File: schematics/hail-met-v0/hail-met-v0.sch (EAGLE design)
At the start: 110 parts, among them IC1 MCP73871, J1 AVR_SPI_PRG_6PTH, U1 ATMEGA328P, Y1 16MHZ

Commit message: ordered pcb
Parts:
- renumbered LED0-IR to LED4-IR
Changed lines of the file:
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@@
 <?xml version="1.0" encoding="utf-8"?>
 <!DOCTYPE eagle SYSTEM "eagle.dtd">
-<eagle version="7.1.0">
+<eagle version="6.5.0">
 <drawing>
 <settings>
@@
 <part name="LED7-CS" library="SparkFun-Connectors" deviceset="M02" device="PTH"/>
 <part name="LED0-IL" library="SparkFun-Connectors" deviceset="M02" device="PTH"/>
-<part name="LED0-IR" library="SparkFun-Connectors" deviceset="M02" device="PTH"/>
+<part name="LED4-IR" library="SparkFun-Connectors" deviceset="M02" device="PTH"/>
 <part name="LED_CREE" library="SparkFun-Connectors" deviceset="M02" device="PTH"/>
 <part name="P+8" library="SparkFun" deviceset="3.3V" device=""/>
@@
 <instance part="LED7-CS" gate="G$1" x="167.64" y="-83.82" rot="R180"/>
 <instance part="LED0-IL" gate="G$1" x="142.24" y="-22.86" rot="R180"/>
-<instance part="LED0-IR" gate="G$1" x="167.64" y="-22.86" rot="R180"/>
+<instance part="LED4-IR" gate="G$1" x="167.64" y="-22.86" rot="R180"/>
 <instance part="LED_CREE" gate="G$1" x="99.06" y="-15.24" rot="R180"/>
 <instance part="P+8" gate="G$1" x="127" y="-38.1"/>
@@
 </segment>
 <segment>
-<pinref part="LED0-IR" gate="G$1" pin="1"/>
+<pinref part="LED4-IR" gate="G$1" pin="1"/>
 <pinref part="P+17" gate="G$1" pin="3.3V"/>
 <wire x1="160.02" y1="-22.86" x2="154.94" y2="-22.86" width="0.1524" layer="91"/>
@@
 <net name="N$66" class="0">
 <segment>
-<pinref part="LED0-IR" gate="G$1" pin="2"/>
+<pinref part="LED4-IR" gate="G$1" pin="2"/>
 <pinref part="R23" gate="G$1" pin="1"/>
 </segment>

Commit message: updated schematics (v0, v1) and datasheets
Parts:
- R11: value 100K -> 8K
- R3: value (none) -> 270K
- R4: value (none) -> 100K
- RT1: value (none) -> 0
- RT2: value (none) -> 80K
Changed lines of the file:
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@@
 <?xml version="1.0" encoding="utf-8"?>
 <!DOCTYPE eagle SYSTEM "eagle.dtd">
-<eagle version="6.5.0">
+<eagle version="7.1.0">
 <drawing>
 <settings>
@@
 <part name="R5" library="SparkFun-Passives" deviceset="RESISTOR" device="0805-RES" value="10K"/>
 <part name="R6" library="SparkFun-Passives" deviceset="RESISTOR" device="0805-RES" value="10K"/>
-<part name="R3" library="SparkFun-Passives" deviceset="RESISTOR" device="0805-RES"/>
-<part name="R4" library="SparkFun-Passives" deviceset="RESISTOR" device="0805-RES"/>
+<part name="R3" library="SparkFun-Passives" deviceset="RESISTOR" device="0805-RES" value="270K"/>
+<part name="R4" library="SparkFun-Passives" deviceset="RESISTOR" device="0805-RES" value="100K"/>
 <part name="R7" library="SparkFun-Passives" deviceset="RESISTOR" device="0805-RES" value="2K"/>
-<part name="R11" library="SparkFun-Passives" deviceset="RESISTOR" device="0805-RES" value="100K"/>
-<part name="RT1" library="SparkFun-Passives" deviceset="RESISTOR" device="0805-RES"/>
-<part name="RT2" library="SparkFun-Passives" deviceset="RESISTOR" device="0805-RES"/>
+<part name="R11" library="SparkFun-Passives" deviceset="RESISTOR" device="0805-RES" value="8K"/>
+<part name="RT1" library="SparkFun-Passives" deviceset="RESISTOR" device="0805-RES" value="0"/>
+<part name="RT2" library="SparkFun-Passives" deviceset="RESISTOR" device="0805-RES" value="80K"/>
 <part name="C7" library="SparkFun-Passives" deviceset="CAP" device="0805" value="10uF"/>
 <part name="C8" library="SparkFun-Passives" deviceset="CAP" device="0805" value="22pF"/>

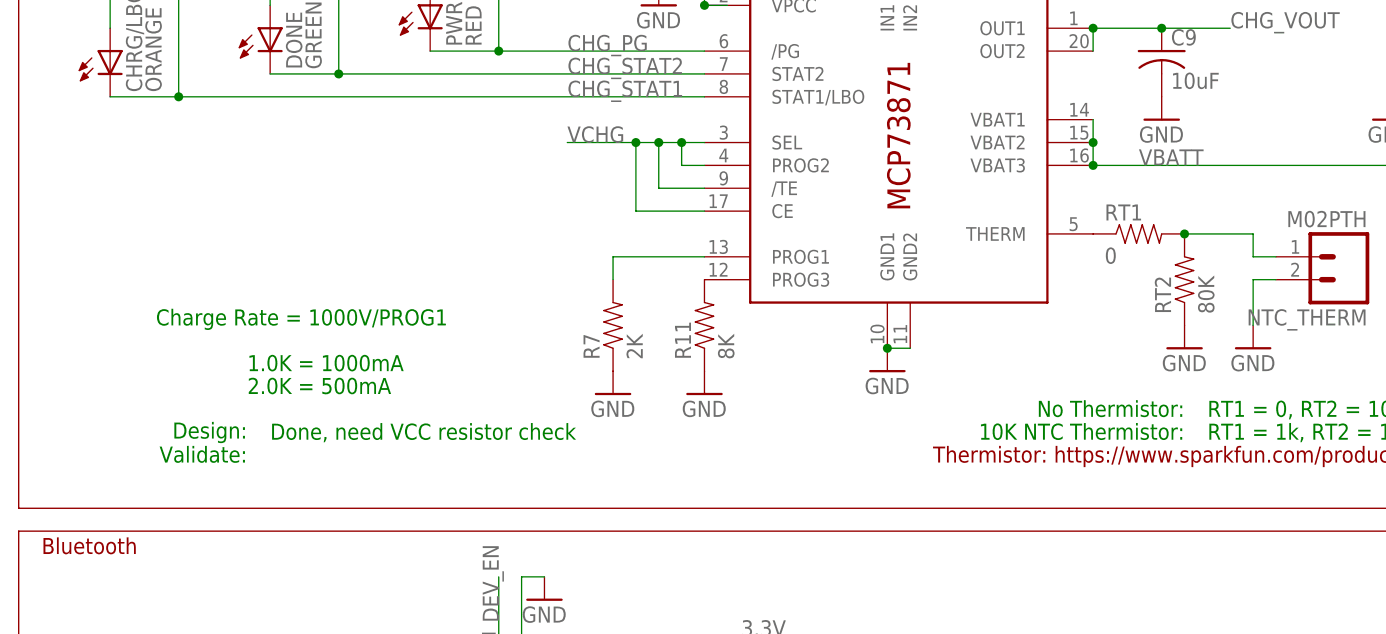
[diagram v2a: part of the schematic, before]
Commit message: updated schematic with charge termination current resistor
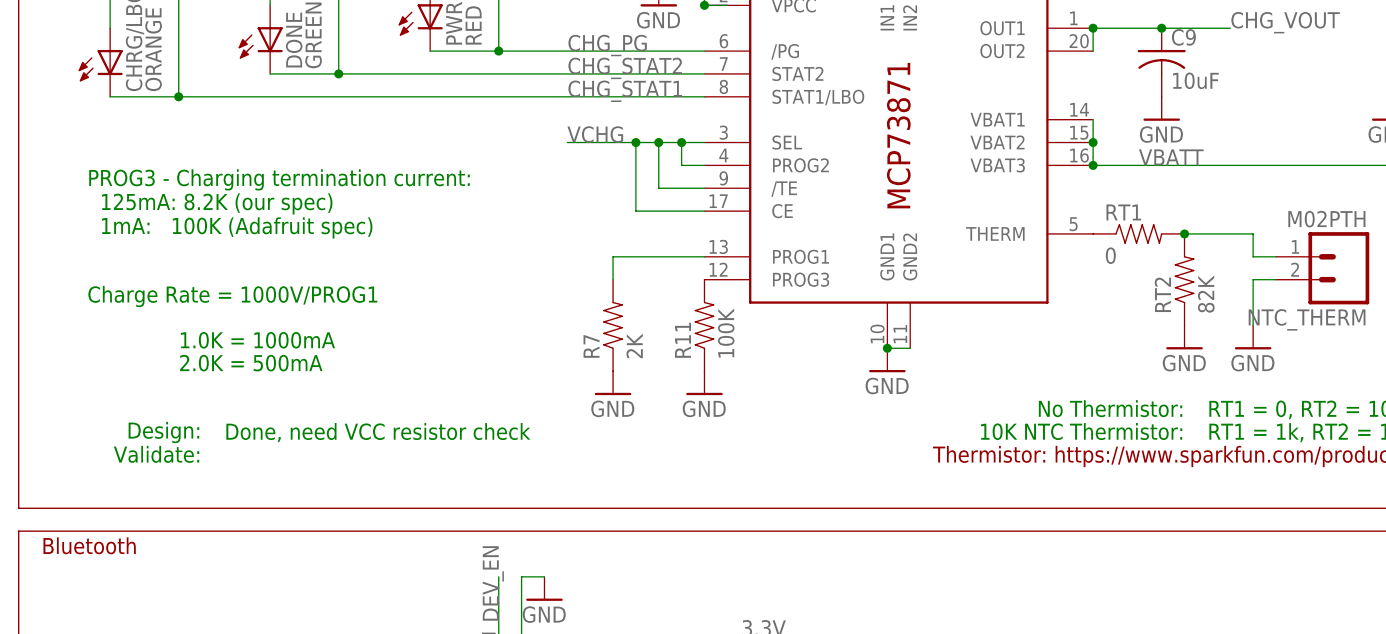
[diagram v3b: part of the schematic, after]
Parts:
- R11: value 8K -> 100K
- RT2: value 80K -> 82K
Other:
- note added: "PROG3 - Charging termination current: 125mA: 8.2K (our spec) 1mA: 100K (Adafruit spec)"
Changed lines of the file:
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@@
 <part name="R4" library="SparkFun-Passives" deviceset="RESISTOR" device="0805-RES" value="100K"/>
 <part name="R7" library="SparkFun-Passives" deviceset="RESISTOR" device="0805-RES" value="2K"/>
-<part name="R11" library="SparkFun-Passives" deviceset="RESISTOR" device="0805-RES" value="8K"/>
+<part name="R11" library="SparkFun-Passives" deviceset="RESISTOR" device="0805-RES" value="100K"/>
 <part name="RT1" library="SparkFun-Passives" deviceset="RESISTOR" device="0805-RES" value="0"/>
-<part name="RT2" library="SparkFun-Passives" deviceset="RESISTOR" device="0805-RES" value="80K"/>
+<part name="RT2" library="SparkFun-Passives" deviceset="RESISTOR" device="0805-RES" value="82K"/>
 <part name="C7" library="SparkFun-Passives" deviceset="CAP" device="0805" value="10uF"/>
 <part name="C8" library="SparkFun-Passives" deviceset="CAP" device="0805" value="22pF"/>
@@
 <text x="-55.88" y="5.08" size="1.778" layer="91" distance="5">RT1 = 0, RT2 = 10K</text>
 <text x="-55.88" y="2.54" size="1.778" layer="91" distance="5">RT1 = 1k, RT2 = 150k</text>
-<text x="-172.72" y="15.24" size="1.778" layer="91" distance="5">Charge Rate = 1000V/PROG1</text>
-<text x="-162.56" y="10.16" size="1.778" layer="91" distance="5">1.0K = 1000mA</text>
-<text x="-162.56" y="7.62" size="1.778" layer="91" distance="5">2.0K = 500mA</text>
+<text x="-180.34" y="17.78" size="1.778" layer="91" distance="5">Charge Rate = 1000V/PROG1</text>
+<text x="-170.18" y="12.7" size="1.778" layer="91" distance="5">1.0K = 1000mA</text>
+<text x="-170.18" y="10.16" size="1.778" layer="91" distance="5">2.0K = 500mA</text>
 <text x="-111.76" y="71.12" size="1.778" layer="91" distance="5">NEED TO SET THIS TO VREG.
 For 6V solar panel, use 1KOhm / 1KOhm</text>
@@
 <text x="12.7" y="60.96" size="1.778" layer="91" align="bottom-right">Design:
 Validate:</text>
-<text x="-162.56" y="0" size="1.778" layer="91" align="bottom-right">Design:
+<text x="-167.64" y="0" size="1.778" layer="91" align="bottom-right">Design:
 Validate:</text>
 <text x="68.58" y="-96.52" size="1.778" layer="91" align="bottom-right">Design:
@@
 <wire x1="220.98" y1="-106.68" x2="53.34" y2="-106.68" width="0.1524" layer="94"/>
 <wire x1="53.34" y1="-106.68" x2="53.34" y2="-7.62" width="0.1524" layer="94"/>
-<text x="-160.02" y="2.54" size="1.778" layer="91">Done, need VCC resistor check</text>
+<text x="-165.1" y="2.54" size="1.778" layer="91">Done, need VCC resistor check</text>
 <wire x1="-187.96" y1="-7.62" x2="50.8" y2="-7.62" width="0.1524" layer="94"/>
 <wire x1="50.8" y1="-7.62" x2="50.8" y2="-106.68" width="0.1524" layer="94"/>
@@
 from solar charging
 circuit to board.</text>
+<text x="-180.34" y="25.4" size="1.778" layer="91">PROG3 - Charging termination current:
+  125mA: 8.2K (our spec)
+  1mA:   100K (Adafruit spec)</text>
 </plain>
 <instances>

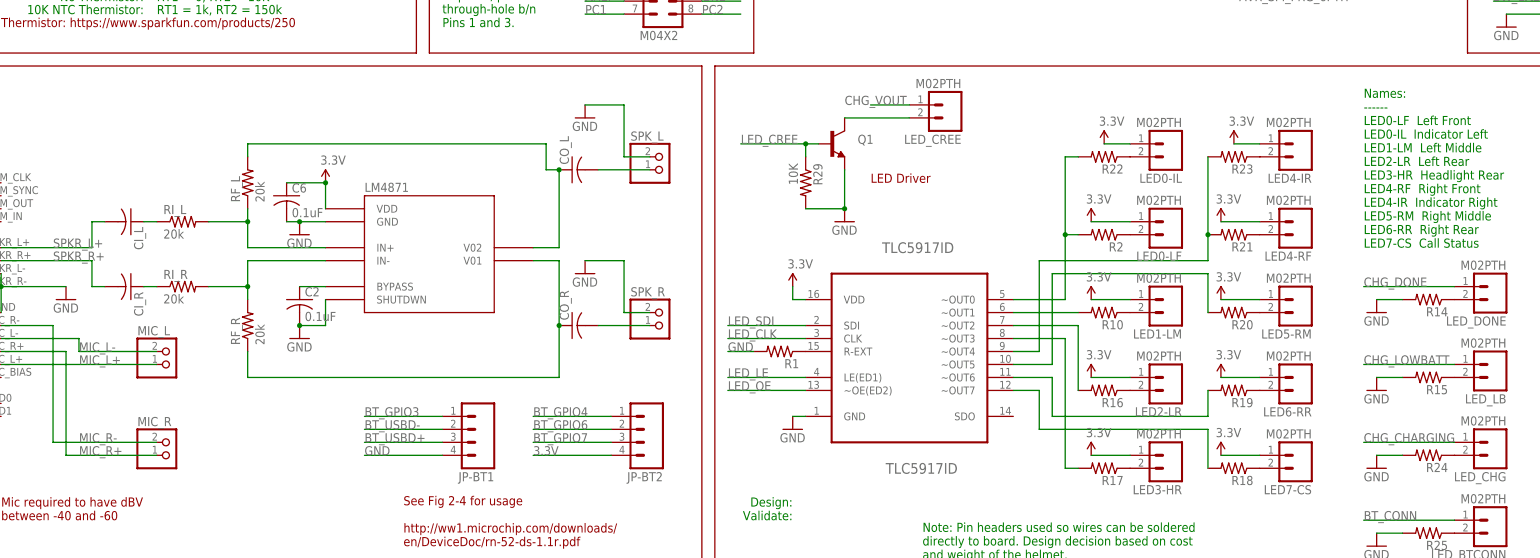
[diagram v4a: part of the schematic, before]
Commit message: modified board with audio amp values
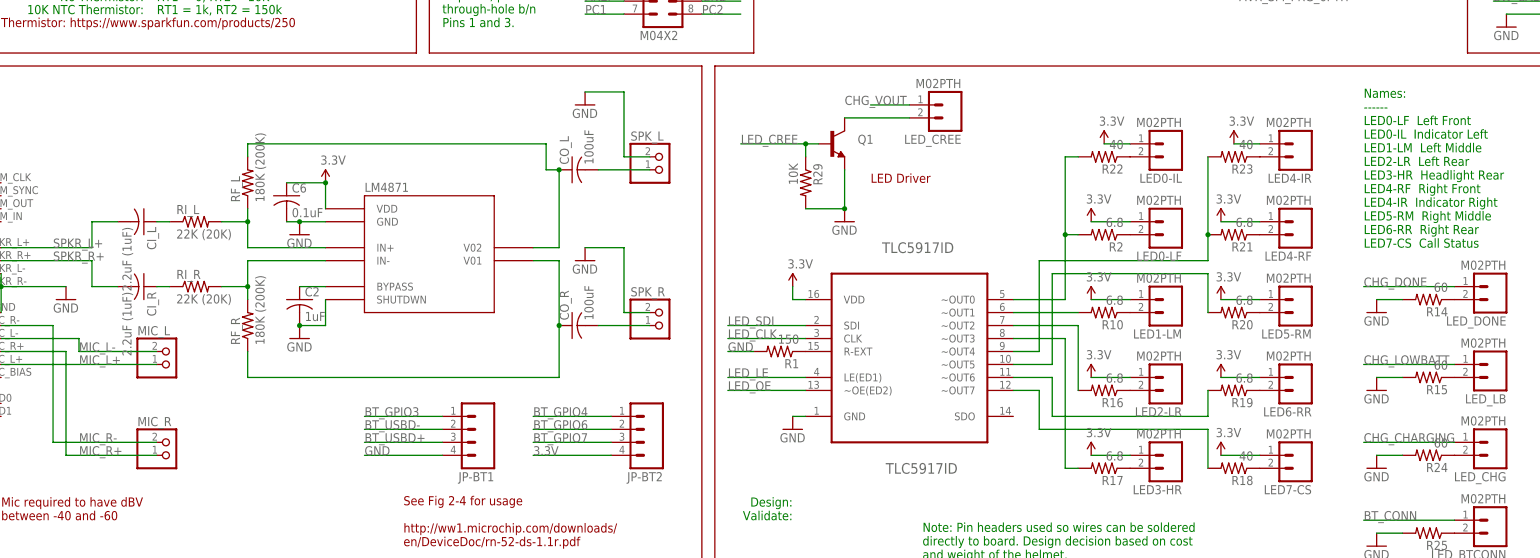
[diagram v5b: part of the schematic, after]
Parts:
- C2: value 0.1uF -> 1uF
- CI_L, CI_R: value (none) -> 2.2uF (1uF)
- CO_L, CO_R: value (none) -> 100uF
- R1: value (none) -> 150
- R10, R16, R17, R19, R2, R20, R21: value (none) -> 6.8
- R14, R15, R24: value (none) -> 60
- R18, R22, R23: value (none) -> 40
- RF_L, RF_R: value 20k -> 180K (200K)
- RI_L, RI_R: value 20k -> 22K (20K)
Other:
- moved on the sheet: CI_L, CI_R, RI_L, RI_R

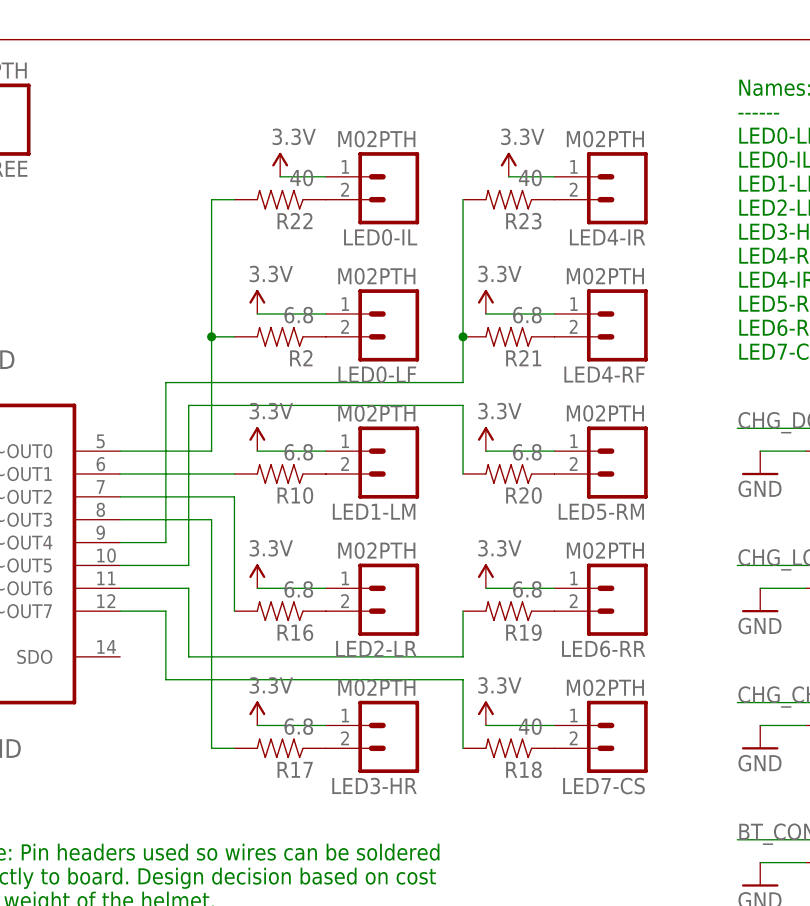
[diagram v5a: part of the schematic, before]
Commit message: updated schematic with new LED driver values
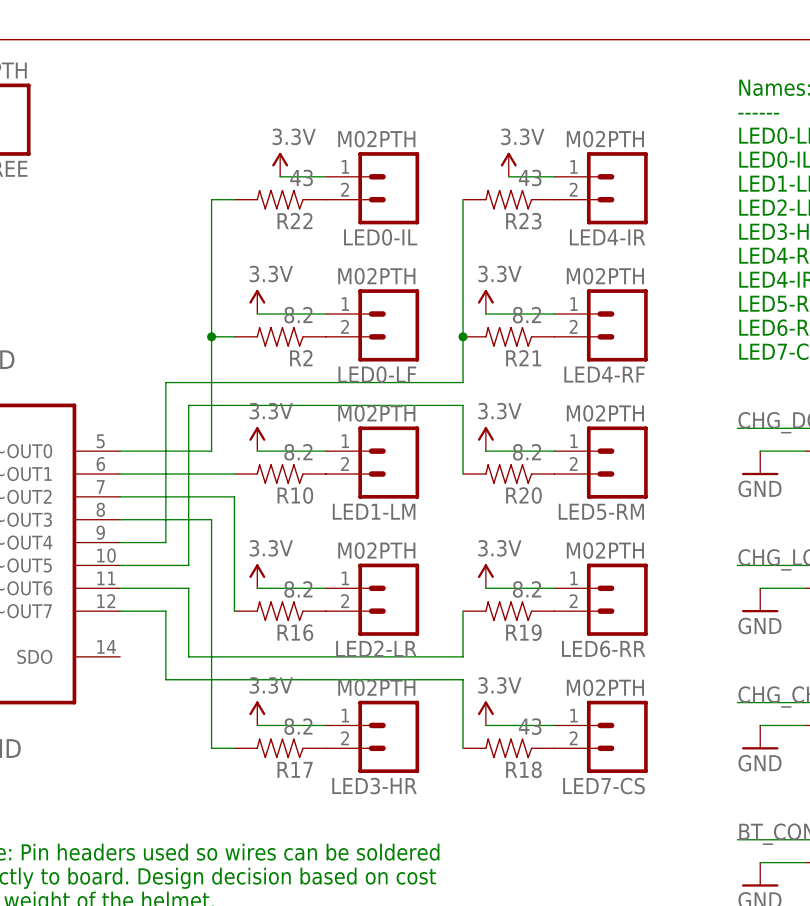
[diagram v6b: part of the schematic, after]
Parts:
- R10, R16, R17, R19, R2, R20, R21: value 6.8 -> 8.2
- R18, R22, R23: value 40 -> 43
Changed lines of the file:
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@@
 <?xml version="1.0" encoding="utf-8"?>
 <!DOCTYPE eagle SYSTEM "eagle.dtd">
-<eagle version="7.1.0">
+<eagle version="7.2.0">
 <drawing>
 <settings>
@@
 <part name="C1" library="SparkFun-Passives" deviceset="CAP" device="0805" value="0.1uF"/>
 <part name="R1" library="SparkFun-Passives" deviceset="RESISTOR" device="0805-RES" value="150"/>
-<part name="R2" library="SparkFun-Passives" deviceset="RESISTOR" device="0805-RES" value="6.8"/>
-<part name="R10" library="SparkFun-Passives" deviceset="RESISTOR" device="0805-RES" value="6.8"/>
-<part name="R16" library="SparkFun-Passives" deviceset="RESISTOR" device="0805-RES" value="6.8"/>
-<part name="R17" library="SparkFun-Passives" deviceset="RESISTOR" device="0805-RES" value="6.8"/>
-<part name="R18" library="SparkFun-Passives" deviceset="RESISTOR" device="0805-RES" value="40"/>
-<part name="R19" library="SparkFun-Passives" deviceset="RESISTOR" device="0805-RES" value="6.8"/>
-<part name="R20" library="SparkFun-Passives" deviceset="RESISTOR" device="0805-RES" value="6.8"/>
-<part name="R21" library="SparkFun-Passives" deviceset="RESISTOR" device="0805-RES" value="6.8"/>
+<part name="R2" library="SparkFun-Passives" deviceset="RESISTOR" device="0805-RES" value="8.2"/>
+<part name="R10" library="SparkFun-Passives" deviceset="RESISTOR" device="0805-RES" value="8.2"/>
+<part name="R16" library="SparkFun-Passives" deviceset="RESISTOR" device="0805-RES" value="8.2"/>
+<part name="R17" library="SparkFun-Passives" deviceset="RESISTOR" device="0805-RES" value="8.2"/>
+<part name="R18" library="SparkFun-Passives" deviceset="RESISTOR" device="0805-RES" value="43"/>
+<part name="R19" library="SparkFun-Passives" deviceset="RESISTOR" device="0805-RES" value="8.2"/>
+<part name="R20" library="SparkFun-Passives" deviceset="RESISTOR" device="0805-RES" value="8.2"/>
+<part name="R21" library="SparkFun-Passives" deviceset="RESISTOR" device="0805-RES" value="8.2"/>
 <part name="FTDI" library="SparkFun-Connectors" deviceset="M06" device="LOCK"/>
-<part name="R22" library="SparkFun-Passives" deviceset="RESISTOR" device="0805-RES" value="40"/>
-<part name="R23" library="SparkFun-Passives" deviceset="RESISTOR" device="0805-RES" value="40"/>
+<part name="R22" library="SparkFun-Passives" deviceset="RESISTOR" device="0805-RES" value="43"/>
+<part name="R23" library="SparkFun-Passives" deviceset="RESISTOR" device="0805-RES" value="43"/>
 <part name="U$3" library="RN52" deviceset="RN52" device=""/>
 <part name="U$2" library="MicroUSB" deviceset="10118193" device=""/>
